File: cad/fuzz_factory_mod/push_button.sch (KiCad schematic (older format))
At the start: 5 parts, among them SW1101 SW_PUSH

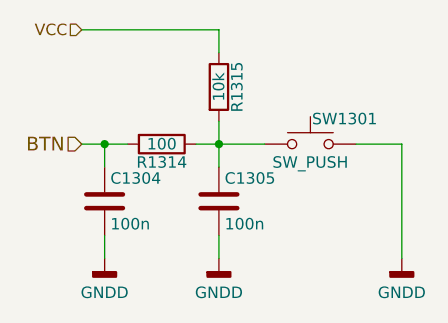
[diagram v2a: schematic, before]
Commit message: Updated trimmers footprint.
Continued layout.
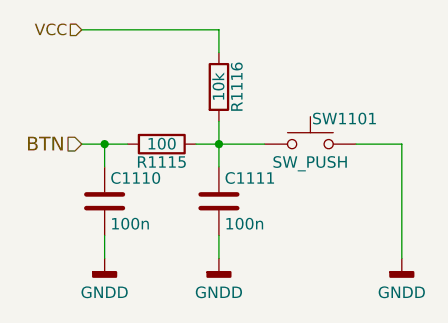
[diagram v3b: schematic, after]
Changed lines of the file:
@@
 $Descr A4 11693 8268
 encoding utf-8
-Sheet 8 22
+Sheet 6 22
 Title ""
 Date ""
@@
 AR Path="/5DE4AD26/5ED20AFC/5ED02FDC" Ref="SW1201"  Part="1"
 AR Path="/5DE4AD26/5ED214FE/5ED02FDC" Ref="SW1301"  Part="1"
-F 0 "SW1301" H 5050 2610 50  0000 C CNN
+F 0 "SW1101" H 5050 2610 50  0000 C CNN
 F 1 "SW_PUSH" H 4900 2420 50  0000 C CNN
 F 2 "Pin_Headers:Pin_Header_Straight_1x02_Pitch2.54mm" H 4900 2500 50  0001 C CNN
@@
 AR Path="/5DE4AD26/5ED20AFC/5ED656A7" Ref="C1207"  Part="1"
 AR Path="/5DE4AD26/5ED214FE/5ED656A7" Ref="C1305"  Part="1"
-F 0 "C1305" H 4525 2850 50  0000 L CNN
+F 0 "C1111" H 4525 2850 50  0000 L CNN
 F 1 "100n" H 4525 2650 50  0000 L CNN
 F 2 "Capacitors_SMD:C_0603" H 4538 2600 50  0001 C CNN
@@
 AR Path="/5DE4AD26/5ED20AFC/5ED656A8" Ref="R1209"  Part="1"
 AR Path="/5DE4AD26/5ED214FE/5ED656A8" Ref="R1314"  Part="1"
-F 0 "R1314" V 4330 2500 50  0000 C CNN
+F 0 "R1115" V 4330 2500 50  0000 C CNN
 F 1 "100" V 4250 2500 50  0000 C CNN
 F 2 "Resistors_SMD:R_0603" V 4180 2500 50  0001 C CNN
@@
 AR Path="/5DE4AD26/5ED20AFC/5ED656AB" Ref="R1210"  Part="1"
 AR Path="/5DE4AD26/5ED214FE/5ED656AB" Ref="R1315"  Part="1"
-F 0 "R1315" V 4580 2250 50  0000 C CNN
+F 0 "R1116" V 4580 2250 50  0000 C CNN
 F 1 "10k" V 4500 2250 50  0000 C CNN
 F 2 "Resistors_SMD:R_0603" V 4430 2250 50  0001 C CNN
@@
 AR Path="/5DE4AD26/5ED20AFC/5ED03006" Ref="C1206"  Part="1"
 AR Path="/5DE4AD26/5ED214FE/5ED03006" Ref="C1304"  Part="1"
-F 0 "C1304" H 4025 2850 50  0000 L CNN
+F 0 "C1110" H 4025 2850 50  0000 L CNN
 F 1 "100n" H 4025 2650 50  0000 L CNN
 F 2 "Capacitors_SMD:C_0603" H 4038 2600 50  0001 C CNN

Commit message: Continued layout.
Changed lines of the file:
@@
 EESchema Schematic File Version 4
-LIBS:fuzz_factory_mod-cache
 EELAYER 30 0
 EELAYER END
@@
 AR Path="/5DE4AD26/5ED20AFC/5ED02FDC" Ref="SW1201"  Part="1"
 AR Path="/5DE4AD26/5ED214FE/5ED02FDC" Ref="SW1301"  Part="1"
-F 0 "SW1101" H 5050 2610 50  0000 C CNN
+F 0 "SW1301" H 5050 2610 50  0000 C CNN
 F 1 "SW_PUSH" H 4900 2420 50  0000 C CNN
 F 2 "Pin_Headers:Pin_Header_Straight_1x02_Pitch2.54mm" H 4900 2500 50  0001 C CNN
@@
 AR Path="/5DE4AD26/5ED20AFC/5ED656A7" Ref="C1207"  Part="1"
 AR Path="/5DE4AD26/5ED214FE/5ED656A7" Ref="C1305"  Part="1"
-F 0 "C1111" H 4525 2850 50  0000 L CNN
+F 0 "C1305" H 4525 2850 50  0000 L CNN
 F 1 "100n" H 4525 2650 50  0000 L CNN
 F 2 "Capacitors_SMD:C_0603" H 4538 2600 50  0001 C CNN
@@
 AR Path="/5DE4AD26/5ED20AFC/5ED656A8" Ref="R1209"  Part="1"
 AR Path="/5DE4AD26/5ED214FE/5ED656A8" Ref="R1314"  Part="1"
-F 0 "R1115" V 4330 2500 50  0000 C CNN
+F 0 "R1314" V 4330 2500 50  0000 C CNN
 F 1 "100" V 4250 2500 50  0000 C CNN
 F 2 "Resistors_SMD:R_0603" V 4180 2500 50  0001 C CNN
@@
 AR Path="/5DE4AD26/5ED20AFC/5ED656AB" Ref="R1210"  Part="1"
 AR Path="/5DE4AD26/5ED214FE/5ED656AB" Ref="R1315"  Part="1"
-F 0 "R1116" V 4580 2250 50  0000 C CNN
+F 0 "R1315" V 4580 2250 50  0000 C CNN
 F 1 "10k" V 4500 2250 50  0000 C CNN
 F 2 "Resistors_SMD:R_0603" V 4430 2250 50  0001 C CNN
@@
 AR Path="/5DE4AD26/5ED20AFC/5ED03006" Ref="C1206"  Part="1"
 AR Path="/5DE4AD26/5ED214FE/5ED03006" Ref="C1304"  Part="1"
-F 0 "C1110" H 4025 2850 50  0000 L CNN
+F 0 "C1304" H 4025 2850 50  0000 L CNN
 F 1 "100n" H 4025 2650 50  0000 L CNN
 F 2 "Capacitors_SMD:C_0603" H 4038 2600 50  0001 C CNN

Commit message: Continued layout.
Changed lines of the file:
@@
 $Descr A4 11693 8268
 encoding utf-8
-Sheet 6 22
+Sheet 7 22
 Title ""
 Date ""
@@
 AR Path="/5DE4AD26/5ED20AFC/5ED02FDC" Ref="SW1201"  Part="1"
 AR Path="/5DE4AD26/5ED214FE/5ED02FDC" Ref="SW1301"  Part="1"
-F 0 "SW1301" H 5050 2610 50  0000 C CNN
+F 0 "SW1201" H 5050 2610 50  0000 C CNN
 F 1 "SW_PUSH" H 4900 2420 50  0000 C CNN
 F 2 "Pin_Headers:Pin_Header_Straight_1x02_Pitch2.54mm" H 4900 2500 50  0001 C CNN
@@
 AR Path="/5DE4AD26/5ED20AFC/5ED656A7" Ref="C1207"  Part="1"
 AR Path="/5DE4AD26/5ED214FE/5ED656A7" Ref="C1305"  Part="1"
-F 0 "C1305" H 4525 2850 50  0000 L CNN
+F 0 "C1207" H 4525 2850 50  0000 L CNN
 F 1 "100n" H 4525 2650 50  0000 L CNN
 F 2 "Capacitors_SMD:C_0603" H 4538 2600 50  0001 C CNN
@@
 AR Path="/5DE4AD26/5ED20AFC/5ED656A8" Ref="R1209"  Part="1"
 AR Path="/5DE4AD26/5ED214FE/5ED656A8" Ref="R1314"  Part="1"
-F 0 "R1314" V 4330 2500 50  0000 C CNN
+F 0 "R1209" V 4330 2500 50  0000 C CNN
 F 1 "100" V 4250 2500 50  0000 C CNN
 F 2 "Resistors_SMD:R_0603" V 4180 2500 50  0001 C CNN
@@
 AR Path="/5DE4AD26/5ED20AFC/5ED656A9" Ref="#PWR01211"  Part="1"
 AR Path="/5DE4AD26/5ED214FE/5ED656A9" Ref="#PWR01307"  Part="1"
-F 0 "#PWR01307" H 4500 2750 50  0001 C CNN
+F 0 "#PWR01211" H 4500 2750 50  0001 C CNN
 F 1 "GNDD" H 4500 2850 50  0000 C CNN
 F 2 "" H 4500 3000 50  0000 C CNN
@@
 AR Path="/5DE4AD26/5ED20AFC/5ED656AA" Ref="#PWR01212"  Part="1"
 AR Path="/5DE4AD26/5ED214FE/5ED656AA" Ref="#PWR01308"  Part="1"
-F 0 "#PWR01308" H 5300 2750 50  0001 C CNN
+F 0 "#PWR01212" H 5300 2750 50  0001 C CNN
 F 1 "GNDD" H 5300 2850 50  0000 C CNN
 F 2 "" H 5300 3000 50  0000 C CNN
@@
 AR Path="/5DE4AD26/5ED20AFC/5ED656AB" Ref="R1210"  Part="1"
 AR Path="/5DE4AD26/5ED214FE/5ED656AB" Ref="R1315"  Part="1"
-F 0 "R1315" V 4580 2250 50  0000 C CNN
+F 0 "R1210" V 4580 2250 50  0000 C CNN
 F 1 "10k" V 4500 2250 50  0000 C CNN
 F 2 "Resistors_SMD:R_0603" V 4430 2250 50  0001 C CNN
@@
 AR Path="/5DE4AD26/5ED20AFC/5ED03006" Ref="C1206"  Part="1"
 AR Path="/5DE4AD26/5ED214FE/5ED03006" Ref="C1304"  Part="1"
-F 0 "C1304" H 4025 2850 50  0000 L CNN
+F 0 "C1206" H 4025 2850 50  0000 L CNN
 F 1 "100n" H 4025 2650 50  0000 L CNN
 F 2 "Capacitors_SMD:C_0603" H 4038 2600 50  0001 C CNN
@@
 AR Path="/5DE4AD26/5ED20AFC/5ED656AD" Ref="#PWR01210"  Part="1"
 AR Path="/5DE4AD26/5ED214FE/5ED656AD" Ref="#PWR01306"  Part="1"
-F 0 "#PWR01306" H 4000 2750 50  0001 C CNN
+F 0 "#PWR01210" H 4000 2750 50  0001 C CNN
 F 1 "GNDD" H 4000 2850 50  0000 C CNN
 F 2 "" H 4000 3000 50  0000 C CNN
